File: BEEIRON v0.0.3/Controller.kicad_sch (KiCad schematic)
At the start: 15 parts, among them SW1 SW_Push, U5 ATmega328P-A, Y1 S3216000091060JY

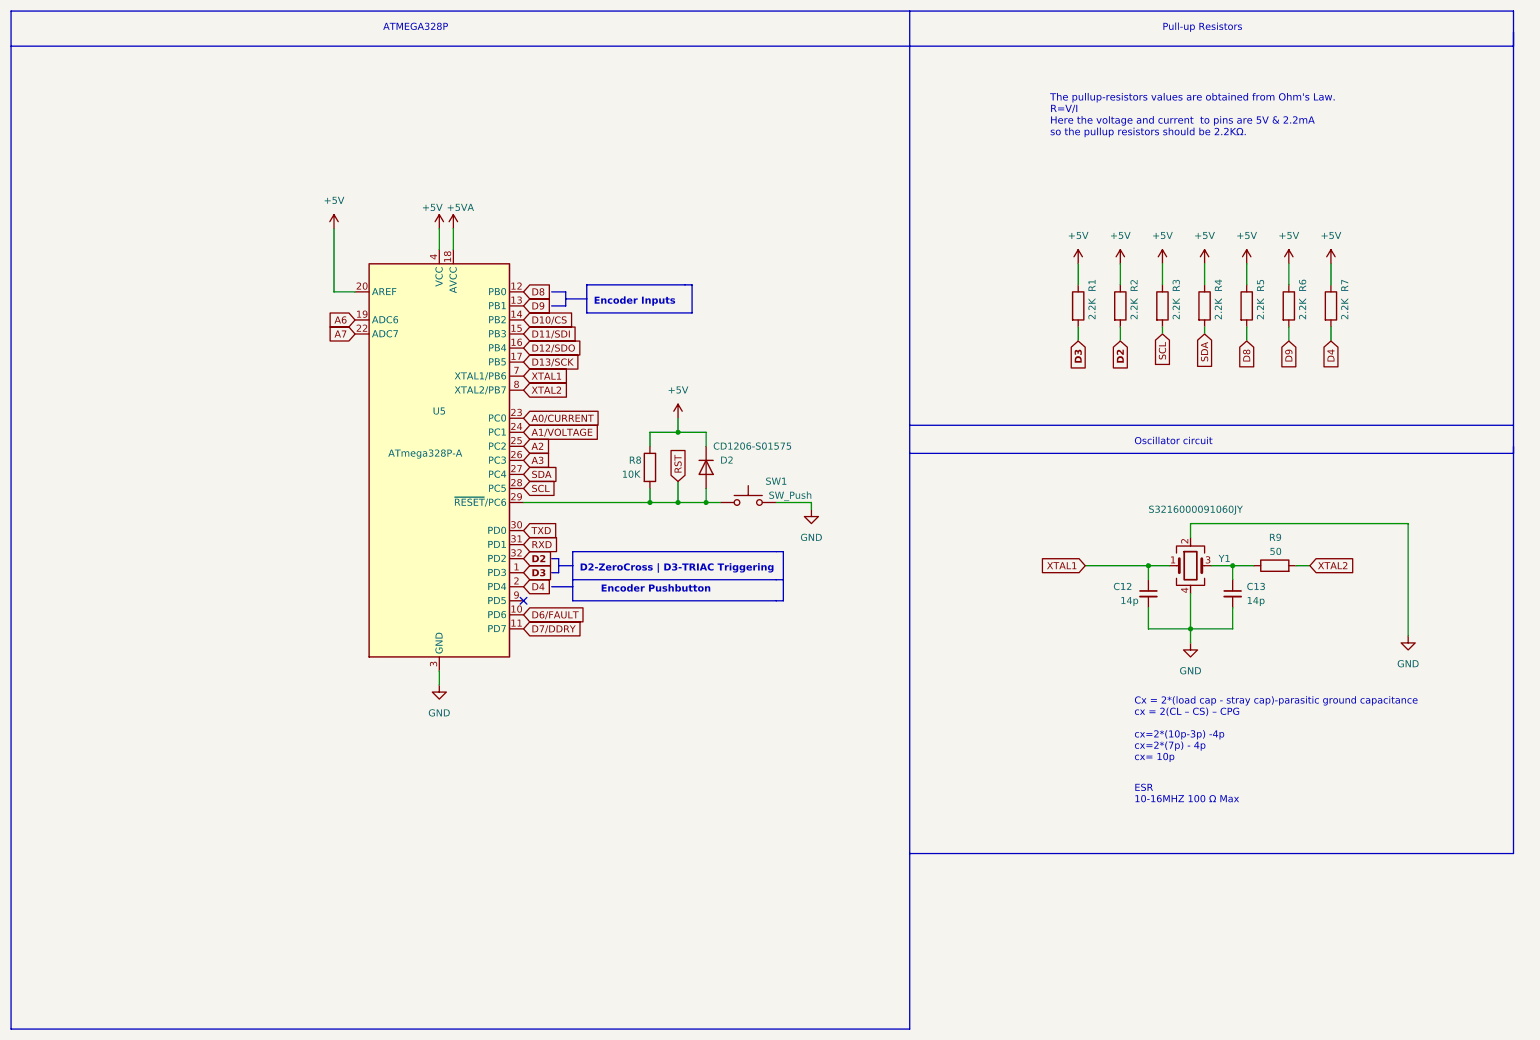
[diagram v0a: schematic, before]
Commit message: added 512K I2C Serial EEPROM support
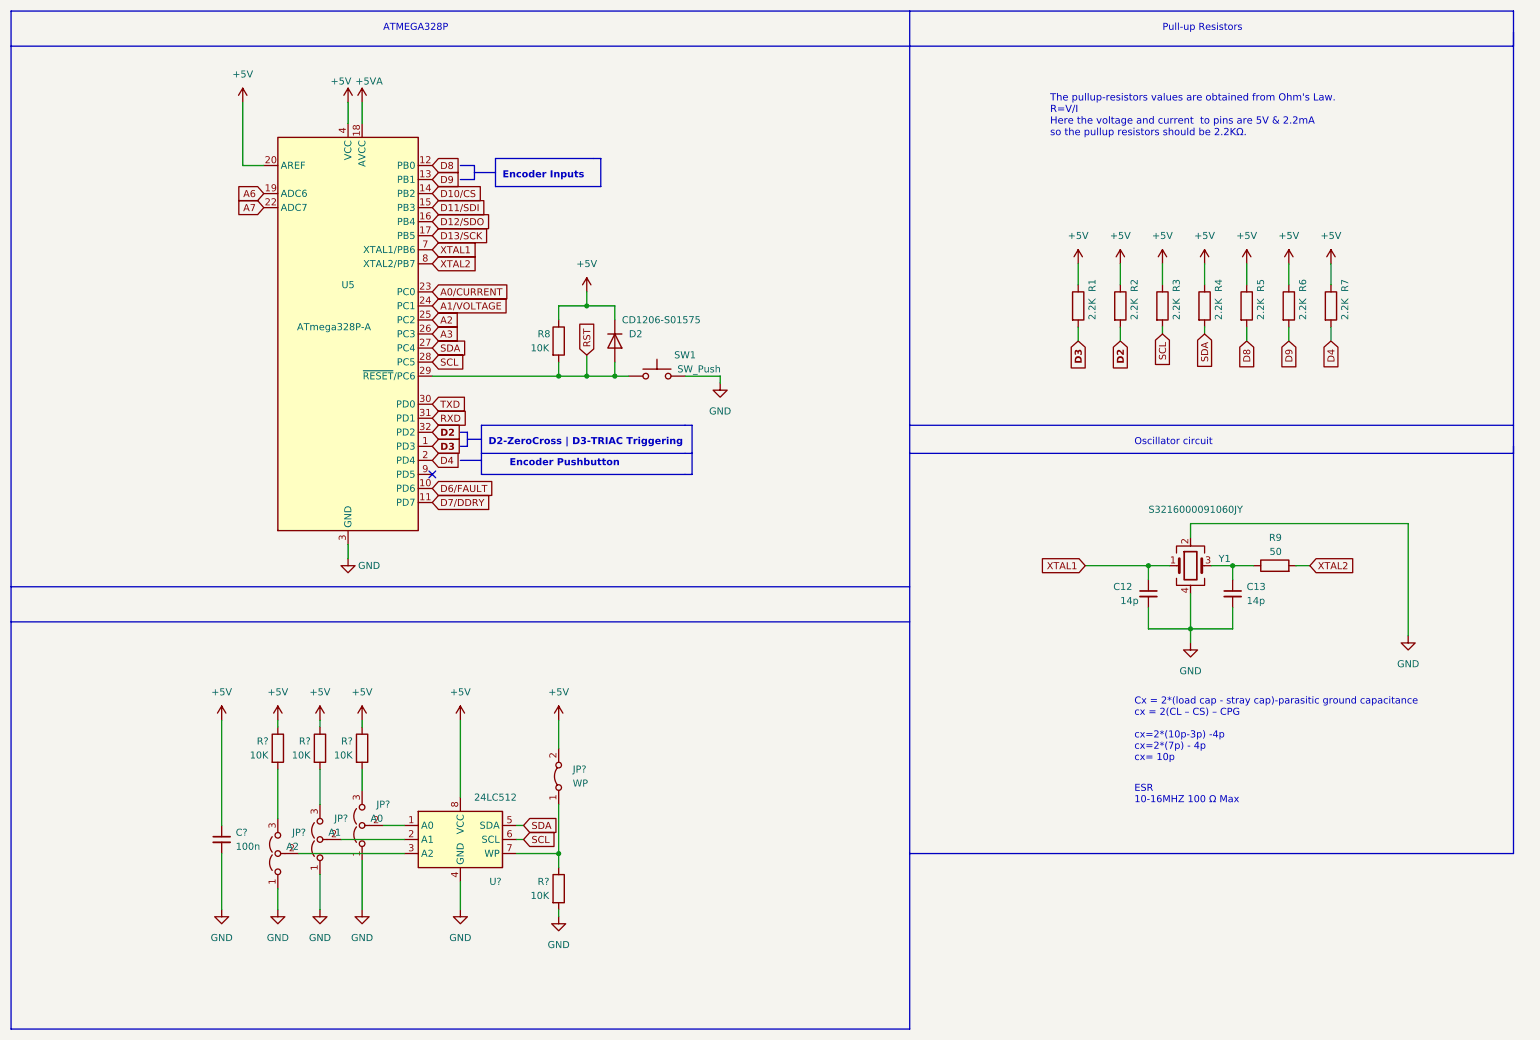
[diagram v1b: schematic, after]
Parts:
- added C?: 100n, Capacitor_SMD:C_0805_2012Metric, symbol Device:C_Small
- added JP?: A0, symbol Jumper:Jumper_3_Open
- added JP?: A1, symbol Jumper:Jumper_3_Open
- added JP?: WP, symbol Jumper:Jumper_2_Bridged
- added JP?: A2, symbol Jumper:Jumper_3_Open
- added R? (x4): 10K, Resistor_SMD:R_0805_2012Metric, symbol Device:R
- added U?: 24LC512, symbol Memory_EEPROM:24LC512
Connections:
- net +5V: now also C?.1, JP?.2 (B), R?.1, R?.1, R?.1, U?.8 (VCC)
- net GND: now also C?.2, JP?.1 (A), JP?.1 (A), JP?.1 (A), R?.2, U?.4 (GND)
- net SCL: now also U?.6 (SCL)
- net SDA: now also U?.5 (SDA)
- new net: JP?.2 (C), U?.1 (A0)
- new net: JP?.3 (B), R?.2 (x3)
- new net: JP?.2 (C), U?.2 (A1)
- new net: JP?.2 (C), U?.3 (A2)
- new net: JP?.1 (A), R?.1, U?.7 (WP)
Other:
- moved on the sheet: D2, R8, SW1, U5
